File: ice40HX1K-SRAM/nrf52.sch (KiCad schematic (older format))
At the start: 3 parts

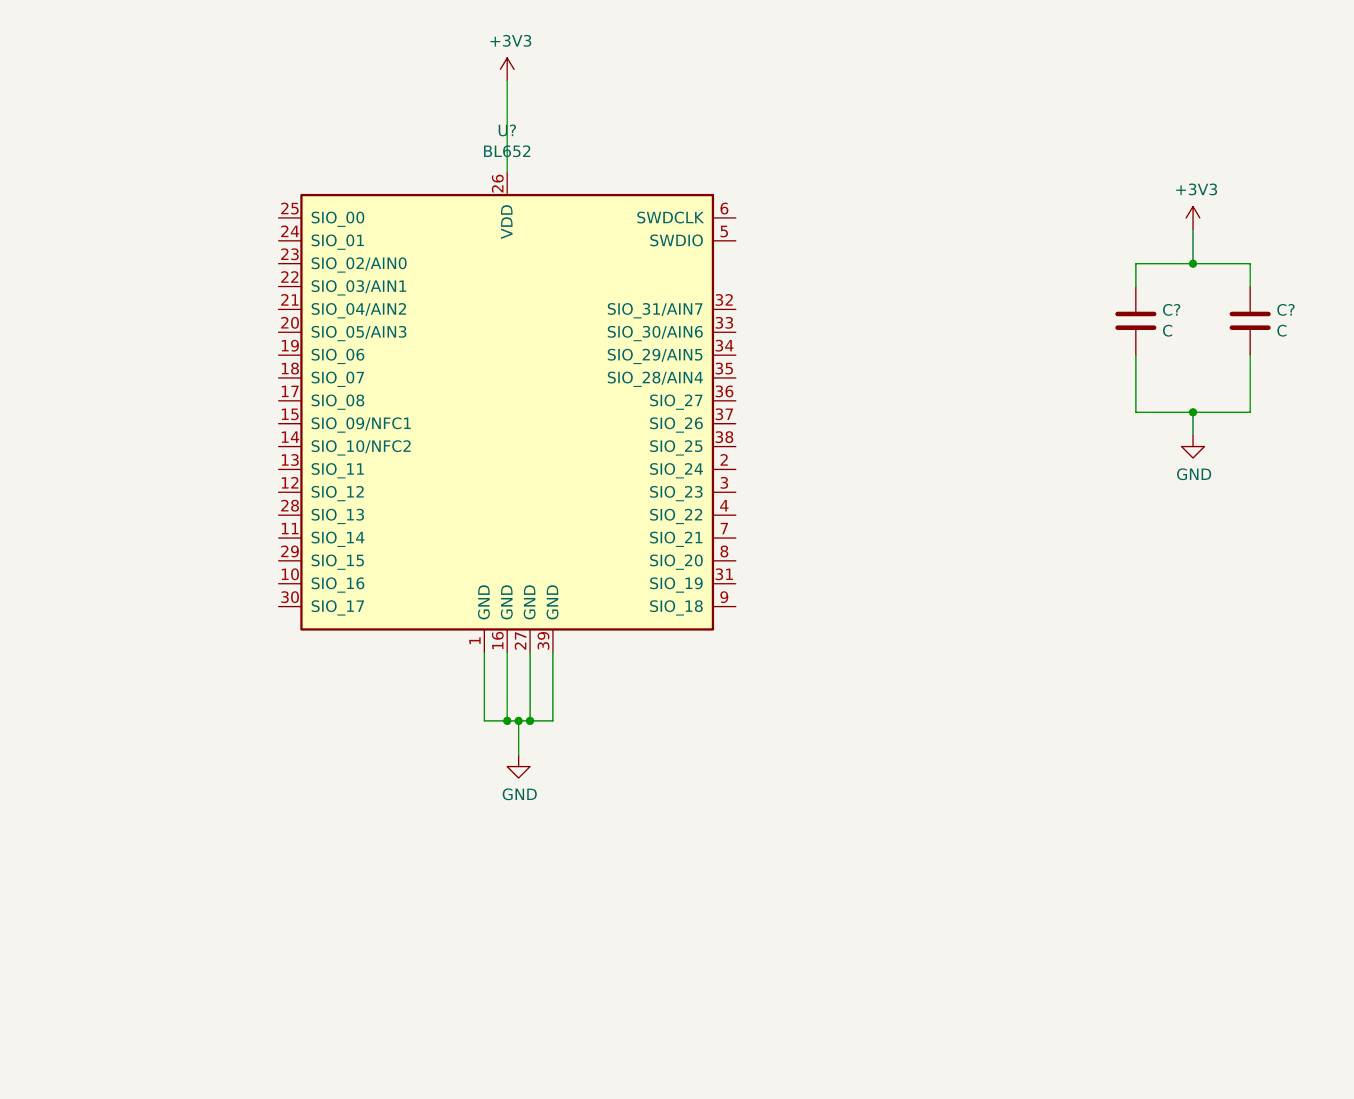
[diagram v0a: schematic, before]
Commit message: wiring FPGA nRF52 and ATSAMD11
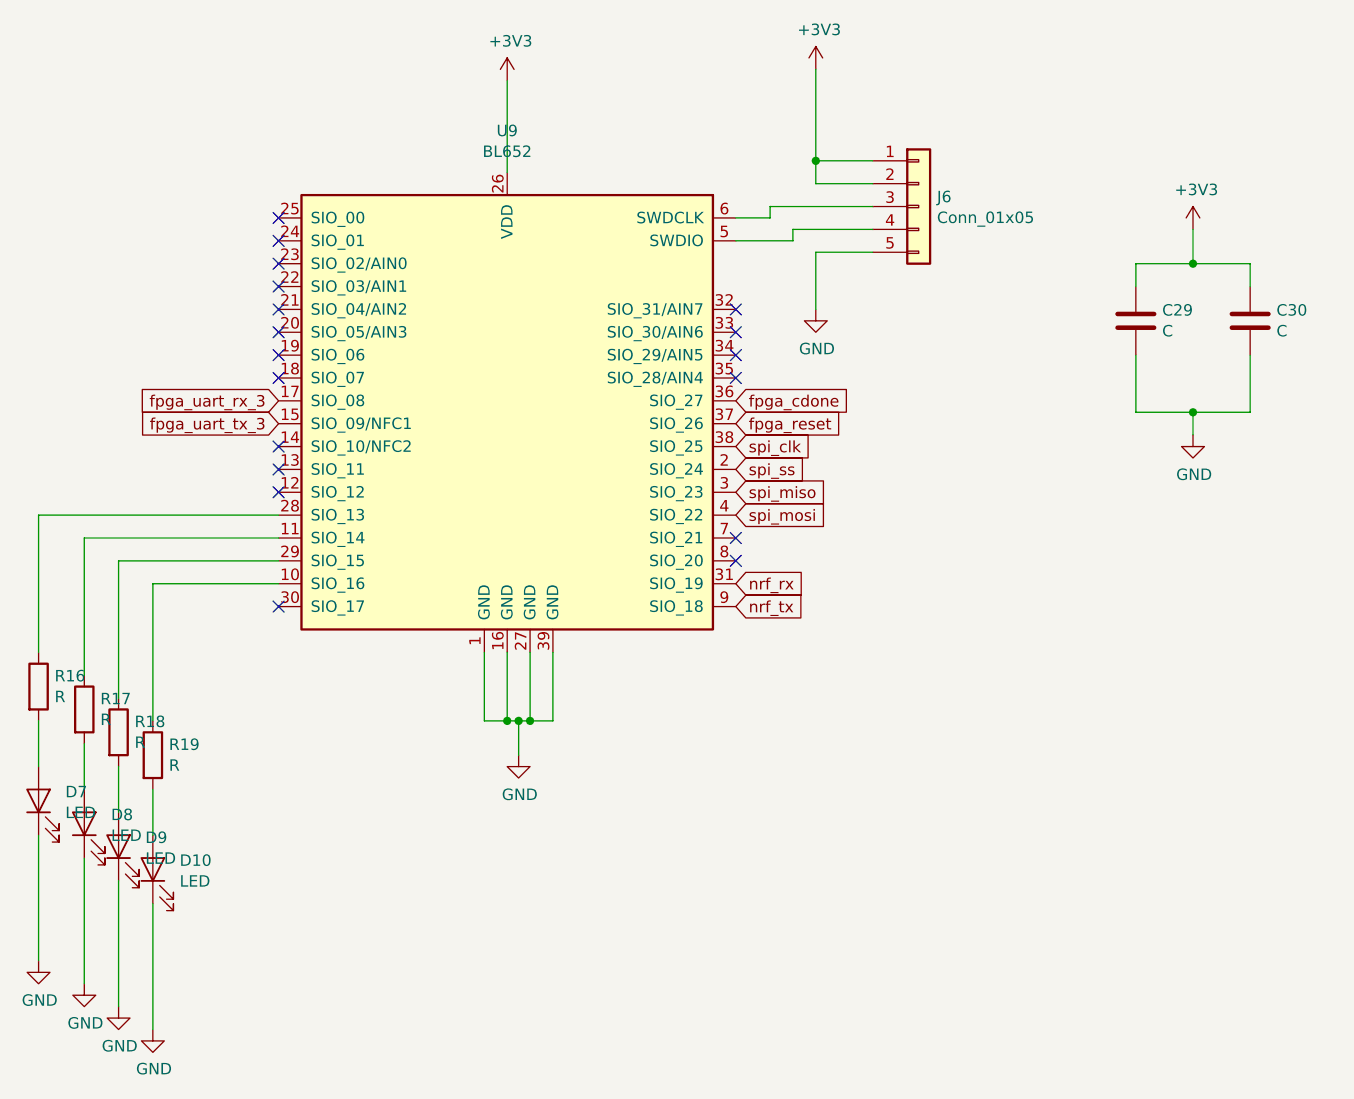
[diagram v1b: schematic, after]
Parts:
- added D10, D7, D8, D9: LED, symbol Device:LED
- added J6: Conn_01x05, symbol Connector_Generic:Conn_01x05
- added R16, R17, R18, R19: R, symbol Device:R
- gave numbers to parts that had none: 3
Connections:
- net +3V3: now also J6.1 (Pin_1), J6.2 (Pin_2)
- net GND: now also D10.1 (K), D7.1 (K), D8.1 (K), D9.1 (K), J6.5 (Pin_5)
- net at U9.10 (SIO_16): now also R19.1
- net at U9.11 (SIO_14): now also R17.1
- net fpga_uart_tx_3: now reaches U9.15 (SIO_09/NFC1)
- net fpga_uart_rx_3: now reaches U9.17 (SIO_08)
- net spi_ss: now reaches U9.2 (SIO_24)
- net at U9.28 (SIO_13): now also R16.1
- net at U9.29 (SIO_15): now also R18.1
- net spi_miso: now reaches U9.3 (SIO_23)
- net nrf_rx: now reaches U9.31 (SIO_19)
- net fpga_cdone: now reaches U9.36 (SIO_27)
- net fpga_reset: now reaches U9.37 (SIO_26)
- net spi_clk: now reaches U9.38 (SIO_25)
- net spi_mosi: now reaches U9.4 (SIO_22)
- net at U9.5 (SWDIO): now also J6.4 (Pin_4)
- net at U9.6 (SWDCLK): now also J6.3 (Pin_3)
- net nrf_tx: now reaches U9.9 (SIO_18)
- new net: D7.2 (A), R16.2
- new net: D8.2 (A), R17.2
- new net: D9.2 (A), R18.2
- new net: D10.2 (A), R19.2
- no-connect marks 0 -> 18

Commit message: wiring FPGA
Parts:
- C29: value C -> 4.7uF; footprint (none) -> Capacitor_SMD:C_0402_1005Metric
- C30: value C -> 0.1uF; footprint (none) -> Capacitor_SMD:C_0402_1005Metric
- J6: footprint (none) -> Connector_PinHeader_2.54mm:PinHeader_1x05_P2.54mm_Vertical
- R16, R17, R18, R19: value R -> 10kOhm; footprint (none) -> Resistor_SMD:R_0402_1005Metric
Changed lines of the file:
@@
 P 7500 3000
 F 0 "C29" H 7615 3046 50  0000 L CNN
-F 1 "C" H 7615 2955 50  0000 L CNN
-F 2 "" H 7538 2850 50  0001 C CNN
+F 1 "4.7uF" H 7615 2955 50  0000 L CNN
+F 2 "Capacitor_SMD:C_0402_1005Metric" H 7538 2850 50  0001 C CNN
 F 3 "~" H 7500 3000 50  0001 C CNN
 	1    7500 3000
@@
 P 8000 3000
 F 0 "C30" H 8115 3046 50  0000 L CNN
-F 1 "C" H 8115 2955 50  0000 L CNN
-F 2 "" H 8038 2850 50  0001 C CNN
+F 1 "0.1uF" H 8115 2955 50  0000 L CNN
+F 2 "Capacitor_SMD:C_0402_1005Metric" H 8038 2850 50  0001 C CNN
 F 3 "~" H 8000 3000 50  0001 C CNN
 	1    8000 3000
@@
 F 0 "J6" H 6630 2542 50  0000 L CNN
 F 1 "Conn_01x05" H 6630 2451 50  0000 L CNN
-F 2 "" H 6550 2500 50  0001 C CNN
+F 2 "Connector_PinHeader_2.54mm:PinHeader_1x05_P2.54mm_Vertical" H 6550 2500 50  0001 C CNN
 F 3 "~" H 6550 2500 50  0001 C CNN
 	1    6550 2500
@@
 P 2700 4600
 F 0 "R16" H 2770 4646 50  0000 L CNN
-F 1 "R" H 2770 4555 50  0000 L CNN
-F 2 "" V 2630 4600 50  0001 C CNN
+F 1 "10kOhm" H 2770 4555 50  0000 L CNN
+F 2 "Resistor_SMD:R_0402_1005Metric" V 2630 4600 50  0001 C CNN
 F 3 "~" H 2700 4600 50  0001 C CNN
 	1    2700 4600
@@
 P 2900 4700
 F 0 "R17" H 2970 4746 50  0000 L CNN
-F 1 "R" H 2970 4655 50  0000 L CNN
-F 2 "" V 2830 4700 50  0001 C CNN
+F 1 "10kOhm" H 2970 4655 50  0000 L CNN
+F 2 "Resistor_SMD:R_0402_1005Metric" V 2830 4700 50  0001 C CNN
 F 3 "~" H 2900 4700 50  0001 C CNN
 	1    2900 4700
@@
 P 3050 4800
 F 0 "R18" H 3120 4846 50  0000 L CNN
-F 1 "R" H 3120 4755 50  0000 L CNN
-F 2 "" V 2980 4800 50  0001 C CNN
+F 1 "10kOhm" H 3120 4755 50  0000 L CNN
+F 2 "Resistor_SMD:R_0402_1005Metric" V 2980 4800 50  0001 C CNN
 F 3 "~" H 3050 4800 50  0001 C CNN
 	1    3050 4800
@@
 P 3200 4900
 F 0 "R19" H 3270 4946 50  0000 L CNN
-F 1 "R" H 3270 4855 50  0000 L CNN
-F 2 "" V 3130 4900 50  0001 C CNN
+F 1 "10kOhm" H 3270 4855 50  0000 L CNN
+F 2 "Resistor_SMD:R_0402_1005Metric" V 3130 4900 50  0001 C CNN
 F 3 "~" H 3200 4900 50  0001 C CNN
 	1    3200 4900

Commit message: starting layout
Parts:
- D10, D7, D8, D9: footprint (none) -> LED_SMD:LED_1206_3216Metric
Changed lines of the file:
@@
 F 0 "D7" V 2739 4983 50  0000 R CNN
 F 1 "LED" V 2648 4983 50  0000 R CNN
-F 2 "" H 2700 5100 50  0001 C CNN
+F 2 "LED_SMD:LED_1206_3216Metric" H 2700 5100 50  0001 C CNN
 F 3 "~" H 2700 5100 50  0001 C CNN
 	1    2700 5100
@@
 F 0 "D8" V 2939 5083 50  0000 R CNN
 F 1 "LED" V 2848 5083 50  0000 R CNN
-F 2 "" H 2900 5200 50  0001 C CNN
+F 2 "LED_SMD:LED_1206_3216Metric" H 2900 5200 50  0001 C CNN
 F 3 "~" H 2900 5200 50  0001 C CNN
 	1    2900 5200
@@
 F 0 "D9" V 3089 5183 50  0000 R CNN
 F 1 "LED" V 2998 5183 50  0000 R CNN
-F 2 "" H 3050 5300 50  0001 C CNN
+F 2 "LED_SMD:LED_1206_3216Metric" H 3050 5300 50  0001 C CNN
 F 3 "~" H 3050 5300 50  0001 C CNN
 	1    3050 5300
@@
 F 0 "D10" V 3239 5283 50  0000 R CNN
 F 1 "LED" V 3148 5283 50  0000 R CNN
-F 2 "" H 3200 5400 50  0001 C CNN
+F 2 "LED_SMD:LED_1206_3216Metric" H 3200 5400 50  0001 C CNN
 F 3 "~" H 3200 5400 50  0001 C CNN
 	1    3200 5400
